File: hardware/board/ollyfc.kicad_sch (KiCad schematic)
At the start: 48 parts, among them J1 Conn_01x06, J12 Conn_01x08, J13 Conn_01x04, J5 Conn_02x05_Odd_Even, Q2 MMBT3904, Q3 MMBT3904, SW2 SW_Push, SW3 SW_Push, SW4 MODE1, SW5 MODE1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

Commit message: v2 files
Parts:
- removed J5: Conn_02x05_Odd_Even, Connector_PinHeader_1.27mm:PinHeader_2x05_P1.27mm_Vertical, symbol Connector_Generic:Conn_02x05_Odd_Even
- removed SW4: MODE1, Button_Switch_SMD:SW_SPDT_PCM12, symbol Switch:SW_SPDT
- added CN1: 20021521-00010T1LF, ofc_sym:IDC-SMD_10P-P1.27_X1270WVS-2X05B-6TV01, symbol ofc_sym:20021521-00010T1LF
- added D5: KT-0603W, ofc_sym:LED0603-R-RD_WHITE, symbol Device:LED_Small
- added J4: Conn_01x05, Connector_JST:JST_PH_B5B-PH-K_1x05_P2.00mm_Vertical, symbol Connector_Generic:Conn_01x05
- added R24: 1K5, Resistor_SMD:R_0402_1005Metric, symbol Device:R_Small
- added TP12, TP13 (x3), TP14 (x3), TP15 (x3), TP16 (x3): TestPoint, TestPoint:TestPoint_Pad_D1.5mm, symbol Connector:TestPoint
- BT1: now left out of the parts list
- C10, C9: footprint ofc_sym:C0402 -> Capacitor_SMD:C_0402_1005Metric; LCSC Part (none) -> C1547
- D1, D3: value STATUS -> KT-0603R; footprint LED_SMD:LED_0603_1608Metric -> ofc_sym:LED0603-RD
- J12, J13: now not fitted; now left out of the parts list
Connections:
- net GYRO_INT3 is gone; now on net MODE1: U3.57 (PB5)
- net +3V3: now also CN1.1
- net BUZZER: now also TP16.1
- net FMEM_CS: now also TP13.1
- net FMEM_HOLD: now also U3.25 (PC5), TP16.1; no longer U3.26 (PB0)
- net GND: now also CN1.3, CN1.5, CN1.9, D5.1 (K), J4.1 (Pin_1)
- net JTCK_SWCLK: now also CN1.4
- net JTDI: now also CN1.8
- net JTDO_SWO: now also CN1.6
- net JTMS_SWDIO: now also CN1.2
- net JTRST: now also CN1.10
- net MODE1: now also SW5.2 (B); no longer U3.27 (PB1)
- net SPI1_MISO: now also TP15.1
- net SPI1_MOSI: now also TP16.1
- net SPI1_SCK: now also TP14.1
- net USART1_RX: now also TP15.1
- net USART1_TX: now also TP13.1
- net USART2_CTS: now also J4.5 (Pin_5), TP12.1
- net USART2_RTS: now also J4.4 (Pin_4), TP14.1
- net USART2_RX: now also J4.2 (Pin_2), TP13.1
- net USART2_TX: now also J4.3 (Pin_3), TP15.1
- net VBAT: now also TP14.1
- net ACCEL_INT1 renamed ACCEL_INT
- net ACCEL_INT2: no longer names the net of U3.2 (PC13)
- net GYRO_INT4 renamed GYRO_INT
- net LED1 renamed STAT_LED
- net LED2 renamed MEM_LED
- net MAG_INT: no longer names the net of U3.24 (PC4)
- net MODE2: no longer names the net of U3.28 (PB2)
- net MODE2: no longer SW5.2 (B)
- new net: D5.2 (A), R24.2
- new net GPS_STATUS: R24.1, U3.26 (PB0)
- no-connect marks 11 -> 16
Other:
- moved on the sheet: R10, R6

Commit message: Re-organize test points. Fix LED footprints #36
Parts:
- D1, D3: footprint ofc_sym:LED0603-RD -> LED_SMD:LED_0603_1608Metric
- D5: footprint ofc_sym:LED0603-R-RD_WHITE -> LED_SMD:LED_0603_1608Metric
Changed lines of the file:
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@@
       (effects (font (size 1.27 1.27)) (justify right))
     )
-    (property "Footprint" "ofc_sym:LED0603-RD" (at 26.67 161.29 90)
+    (property "Footprint" "LED_SMD:LED_0603_1608Metric" (at 26.67 161.29 90)
       (effects (font (size 1.27 1.27)) hide)
     )
@@
       (effects (font (size 1.27 1.27)) (justify right))
     )
-    (property "Footprint" "ofc_sym:LED0603-R-RD_WHITE" (at 66.04 154.305 90)
+    (property "Footprint" "LED_SMD:LED_0603_1608Metric" (at 66.04 154.305 90)
       (effects (font (size 1.27 1.27)) hide)
     )
@@
       (effects (font (size 1.27 1.27)) (justify right))
     )
-    (property "Footprint" "ofc_sym:LED0603-RD" (at 43.815 153.67 90)
-      (effects (font (size 1.27 1.27)) hide)
-    )
+    (property "Footprint" "LED_SMD:LED_0603_1608Metric" (at 43.815 153.67 90)
+      (effects (font (size 1.27 1.27)) hide)
+    )

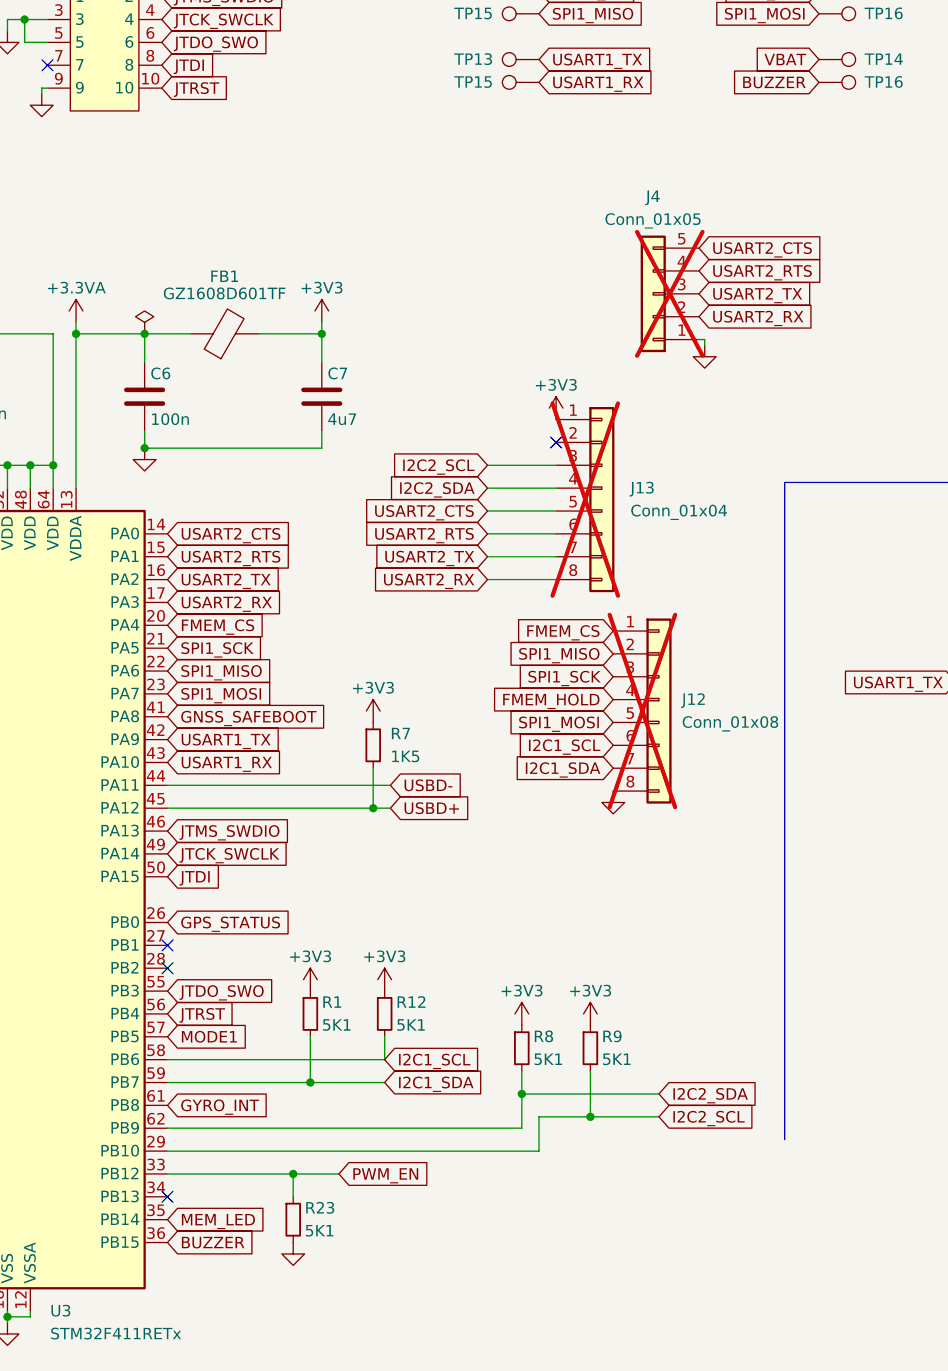
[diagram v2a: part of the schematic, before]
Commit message: Add aux line #36
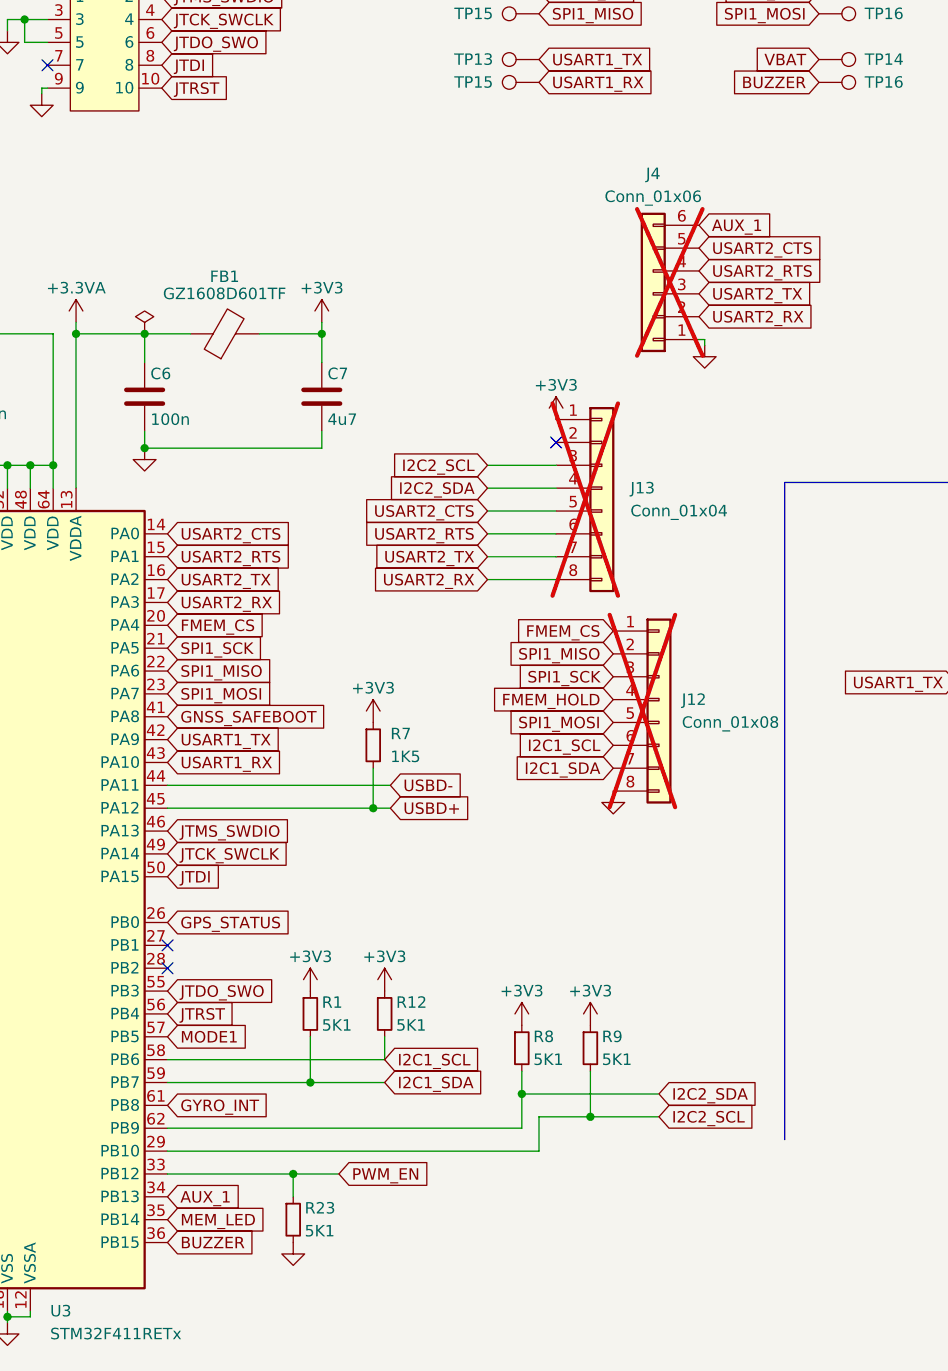
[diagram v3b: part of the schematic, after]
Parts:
- J4: value Conn_01x05 -> Conn_01x06; footprint Connector_JST:JST_PH_B5B-PH-K_1x05_P2.00mm_Vertical -> Connector_JST:JST_PH_B6B-PH-K_1x06_P2.00mm_Vertical; symbol Connector_Generic:Conn_01x05 -> Connector_Generic:Conn_01x06; now in the parts list
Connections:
- net AUX_1: now reaches U3.34 (PB13)
- net AUX_1: now also J4.6 (Pin_6)
- no-connect marks 16 -> 15
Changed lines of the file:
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@@
   (no_connect (at 97.79 116.205))
   (no_connect (at 248.92 62.23))
-  (no_connect (at 133.35 172.085))
   (no_connect (at 133.35 146.685))
   (no_connect (at 97.79 141.605))
@@
     )
   )
+  (global_label "AUX_1" (shape input) (at 133.35 172.085 0) (fields_autoplaced)
+    (effects (font (size 1.27 1.27)) (justify left))
+    (property "Intersheetrefs" "${INTERSHEET_REFS}" (at 142.1409 172.085 0)
+      (effects (font (size 1.27 1.27)) (justify left) hide)
+    )
+  )
   (global_label "USART1_TX" (shape input) (at 220.98 114.935 180) (fields_autoplaced)
     (effects (font (size 1.27 1.27)) (justify right))
@@
     )
   )
+  (global_label "AUX_1" (shape input) (at 192.405 64.135 0) (fields_autoplaced)
+    (effects (font (size 1.27 1.27)) (justify left))
+    (property "Intersheetrefs" "${INTERSHEET_REFS}" (at 201.1959 64.135 0)
+      (effects (font (size 1.27 1.27)) (justify left) hide)
+    )
+  )
   (global_label "FMEM_CS" (shape input) (at 248.92 52.07 180) (fields_autoplaced)
     (effects (font (size 1.27 1.27)) (justify right))
@@
     )
   )
-  (symbol (lib_id "Connector_Generic:Conn_01x05") (at 187.325 71.755 180) (unit 1)
-    (in_bom no) (on_board yes) (dnp yes) (fields_autoplaced)
-    (property "Reference" "J4" (at 187.325 60.96 0)
+  (symbol (lib_id "Connector_Generic:Conn_01x06") (at 187.325 71.755 180) (unit 1)
+    (in_bom yes) (on_board yes) (dnp yes) (fields_autoplaced)
+    (property "Reference" "J4" (at 187.325 58.42 0)
       (effects (font (size 1.27 1.27)))
     )
-    (property "Value" "Conn_01x05" (at 187.325 63.5 0)
+    (property "Value" "Conn_01x06" (at 187.325 60.96 0)
       (effects (font (size 1.27 1.27)))
     )
-    (property "Footprint" "Connector_JST:JST_PH_B5B-PH-K_1x05_P2.00mm_Vertical" (at 187.325 71.755 0)
+    (property "Footprint" "Connector_JST:JST_PH_B6B-PH-K_1x06_P2.00mm_Vertical" (at 187.325 71.755 0)
       (effects (font (size 1.27 1.27)) hide)
     )
@@
     (pin "4")
     (pin "5")
+    (pin "6")
     (instances
       (project "ollyfc"

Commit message: v3 schematic + layout
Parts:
- removed D3: KT-0603R, LED_SMD:LED_0603_1608Metric, symbol Device:LED_Small
- removed D5: KT-0603W, LED_SMD:LED_0603_1608Metric, symbol Device:LED_Small
- removed J1: Conn_01x06, Connector_JST:JST_PH_B6B-PH-K_1x06_P2.00mm_Vertical, symbol Connector_Generic:Conn_01x06
- removed J12: Conn_01x08, Connector_PinHeader_2.54mm:PinHeader_1x08_P2.54mm_Vertical, symbol Connector_Generic:Conn_01x08
- removed J13: Conn_01x04, Connector_PinHeader_2.54mm:PinHeader_1x08_P2.54mm_Vertical, symbol Connector_Generic:Conn_01x08
- removed R24: 1K5, Resistor_SMD:R_0402_1005Metric, symbol Device:R_Small
- removed SW3: SW_Push, Button_Switch_THT:SW_PUSH_6mm, symbol Switch:SW_Push
- removed TP12, TP13 (x3), TP14 (x2), TP15 (x3), TP16 (x3): TestPoint, TestPoint:TestPoint_Pad_D1.5mm, symbol Connector:TestPoint
- added J1: Conn_01x04, Connector_JST:JST_PH_B4B-PH-K_1x04_P2.00mm_Vertical, symbol Connector_Generic:Conn_01x04
- added J3: Conn_01x07, Connector_JST:JST_PH_B7B-PH-K_1x07_P2.00mm_Vertical, symbol Connector_Generic:Conn_01x07
- added R18, R27, R29: 5K1, Resistor_SMD:R_0402_1005Metric, symbol Device:R_Small
- added SW1: MODE1, Button_Switch_SMD:SW_SPDT_PCM12, symbol Switch:SW_SPDT
- added TP14 (x17), TP24 (x8), TP25 (x9): TestPoint, TestPoint:TestPoint_Pad_D1.0mm, symbol Connector:TestPoint
- R10: value 1K5 -> 5K1
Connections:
- net ACCEL_INT is gone; now on net AUX_1: U3.11 (PC3)
- net GPS_STATUS is gone; now on net MAG_DRDY: U3.26 (PB0)
- net PRES_INT is gone; now on net GNSS_TIMEP: U3.9 (PC1)
- net +3V3: now also R10.1, R23.1, J1.2 (Pin_2), J3.1 (Pin_1), R18.2, R27.1, SW1.3 (C)
- net AUX_1: now also TP14.1; no longer U3.34 (PB13)
- net BOOT0: now also SW1.2 (B)
- net BUZZER: now also U3.37 (PC6); no longer U3.36 (PB15)
- net FMEM_HOLD: now also U3.24 (PC4), TP14.1; no longer U3.25 (PC5)
- net GND: now also J1.1 (Pin_1), J3.2 (Pin_2), R29.1; no longer R23.2
- net GNSS_INT: now also U3.8 (PC0); no longer U3.52 (PC11)
- net GNSS_RESET: now also U3.10 (PC2); no longer U3.51 (PC10)
- net GNSS_TIMEP: no longer U3.53 (PC12)
- net I2C1_SCL: now also R8.2, TP24.1; no longer R12.2
- net I2C1_SDA: now also TP25.1
- net I2C2_SCL: now also R23.2, TP25.1; no longer R9.2
- net I2C2_SDA: now also R27.2, TP24.1; no longer R8.2
- net MAG_DRDY: now also TP25.1; no longer U3.8 (PC0)
- net MODE1: now also U3.40 (PC9); no longer U3.57 (PB5)
- net PWM_EN: now also U3.25 (PC5), R18.1, TP25.1; no longer R23.1, U3.33 (PB12)
- net PWR_STATE: now also U3.28 (PB2); no longer U3.37 (PC6)
- net SBUS_OUT: now also J1.4 (Pin_4), TP14.1
- net SPI1_MISO: now also TP14.1
- net SPI1_MOSI: now also TP14.1
- net SPI1_SCK: now also TP14.1
- net STAT_LED: now also U3.39 (PC8); no longer U3.38 (PC7)
- net S_PORT: now also J1.3 (Pin_3), TP14.1
- net USART2_CTS: now also TP14.1
- net USART2_RTS: now also TP14.1
- net USART2_RX: now also TP14.1
- net USART2_TX: now also TP14.1
- net ACC_CS: now reaches U3.2 (PC13)
- net ACC_CS: now also TP25.1
- net DISP_DC: now reaches U3.27 (PB1)
- net DISP_DC: now also J3.7 (Pin_7), TP14.1
- net PRES_DRDY: now reaches U3.3 (PC14)
- net PRES_DRDY: now also TP24.1
- net PRES_CS: now reaches U3.4 (PC15)
- net PRES_CS: now also TP24.1
- net IMU_DRDY: now reaches U3.54 (PD2)
- net IMU_DRDY: now also TP25.1
- net SPI2_NSS: now reaches R10.2
- net SPI2_NSS: now also U3.33 (PB12), J3.5 (Pin_5), TP14.1
- net FMEM_CS renamed SPI1_NSS_EXTF
- net SPI1_NSS_EXTF: now also TP14.1
- net GNSS_SAFEBOOT renamed I2C3_ SCL
- net I2C3_ SCL: now also R9.2, TP24.1
- net GYRO_INT renamed I2C3_SDA
- net I2C3_SDA: now also R12.2, TP25.1
- net MEM_LED renamed SPI2_MISO
- net SPI2_MISO: now also J3.6 (Pin_6), TP14.1; no longer R10.1
- new net: R29.2, SW1.1 (A)
- new net GYR_CS: TP24.1, U3.57 (PB5)
- new net MAG_CS: TP25.1, U3.38 (PC7)
- new net SPI2_MOSI: J3.3 (Pin_3), TP14.1, U3.36 (PB15)
- new net SPI2_SCK: J3.4 (Pin_4), TP14.1, U3.34 (PB13)
- new net SPI3_MISO: TP25.1, U3.52 (PC11)
- new net SPI3_MOSI: TP24.1, U3.53 (PC12)
- new net SPI3_SCK: TP24.1, U3.51 (PC10)
- no-connect marks 15 -> 2
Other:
- note removed: "Mode Switches Status Indicator"
- moved on the sheet: BT1, C1, C10, C11, C2, C3, C4, C5, C6, C7, C8, C9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

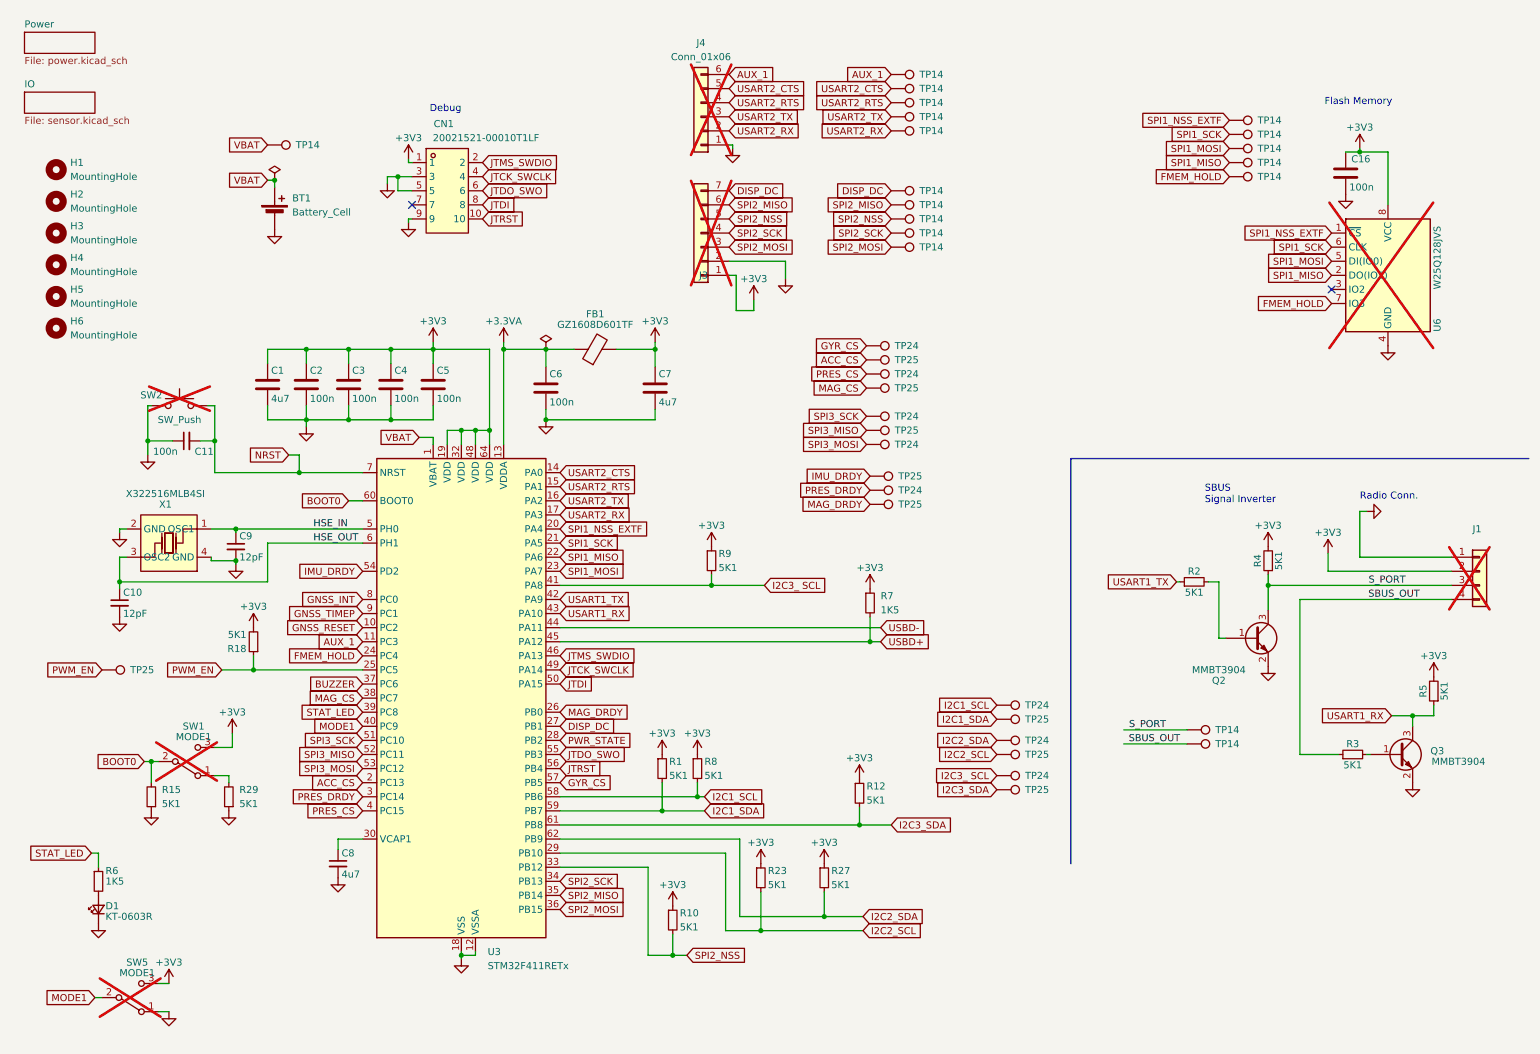
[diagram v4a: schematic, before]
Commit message: Added some organization to schematic
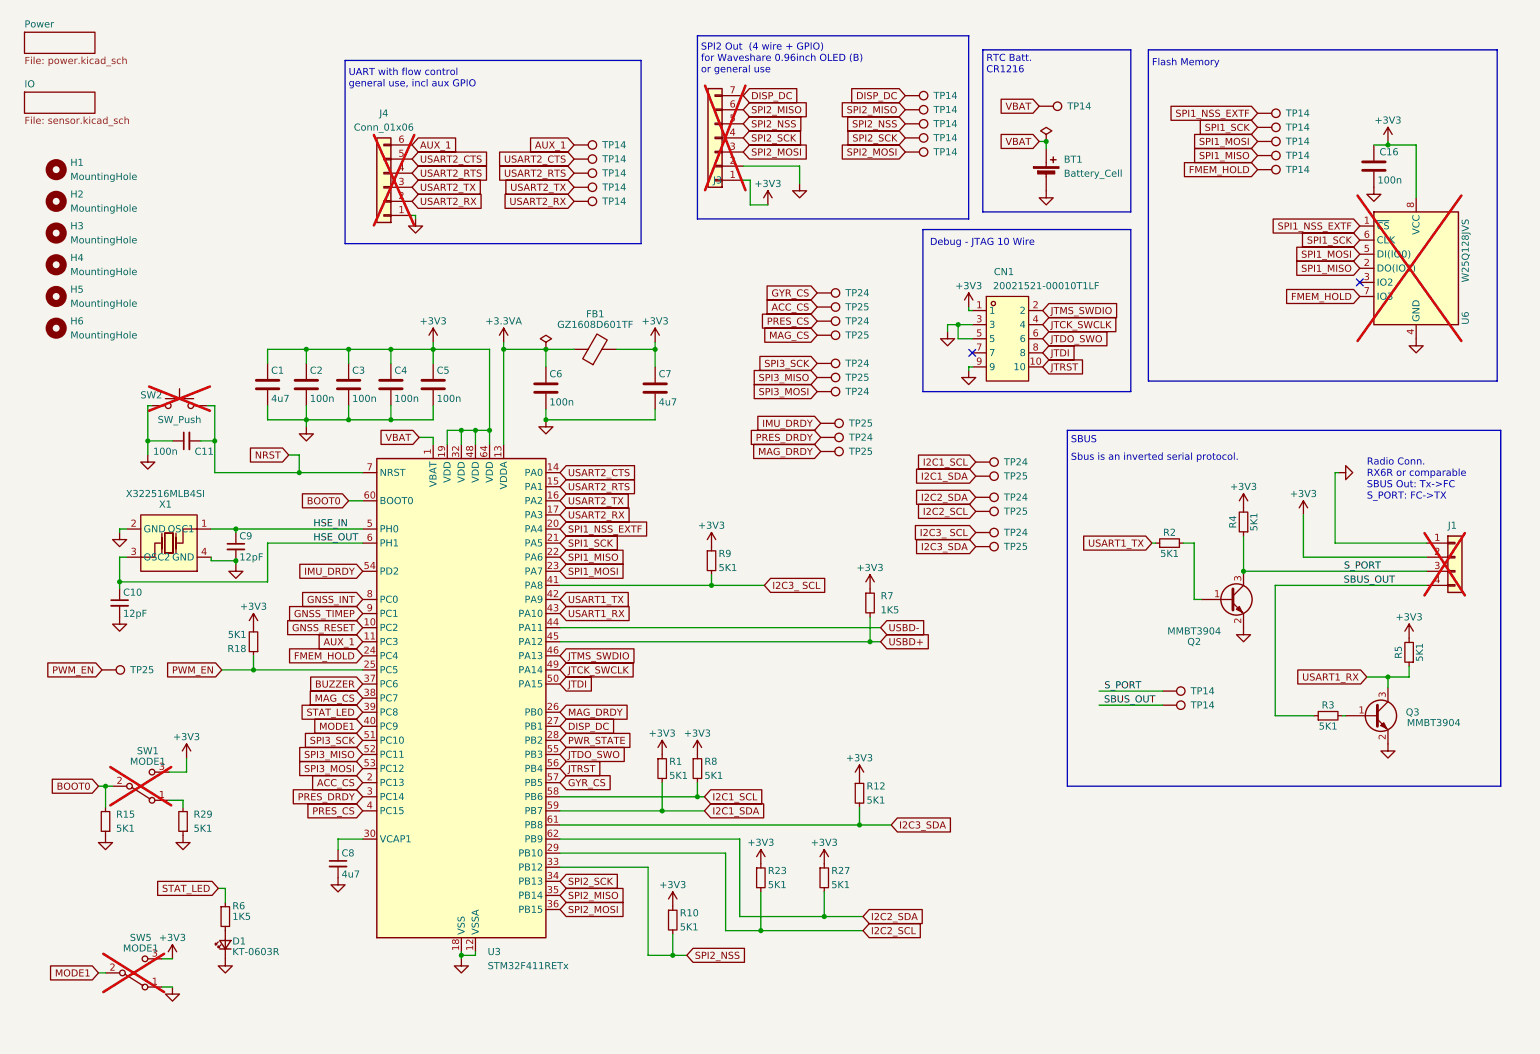
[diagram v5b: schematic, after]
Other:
- note added: "Debug - JTAG 10 Wire"
- note added: "RTC Batt. CR1216"
- note added: "Radio Conn. RX6R or comparable SBUS Out: Tx->FC S_PORT: FC->TX"
- note added: "SBUS"
- note added: "SPI2 Out (4 wire + GPIO) for Waveshare 0.96inch OLED (B) or general use"
- note added: "Sbus is an inverted serial protocol."
- note added: "UART with flow control general use, incl aux GPIO"
- note removed: "Debug"
- note removed: "Radio Conn."
- note removed: "SBUS Signal Inverter"
- moved on the sheet: BT1, C16, CN1, D1, J1, J3, J4, Q2, Q3, R15, R2, R29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
